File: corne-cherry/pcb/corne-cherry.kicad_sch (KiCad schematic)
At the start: 146 parts, among them J1 MJ-4PP-9, J2 OLED, J3 MJ-4PP-9, J4 OLED, SW1 SW_PUSH, SW10 SW_PUSH, SW11 SW_PUSH, SW12 SW_PUSH, SW13 SW_PUSH, SW14 SW_PUSH, SW15 SW_PUSH, SW16 SW_PUSH, SW17 SW_PUSH, SW18 SW_PUSH, SW19 SW_PUSH, SW2 SW_PUSH, SW20 SW_PUSH, SW21 SW_PUSH, SW22 SW_PUSH, SW23 SW_PUSH, SW24 SW_PUSH, SW25 SW_PUSH, SW26 SW_PUSH, SW27 SW_PUSH, SW28 SW_PUSH, SW29 SW_PUSH, SW3 SW_PUSH, SW30 SW_PUSH, SW31 SW_PUSH, SW32 SW_PUSH, SW33 SW_PUSH, SW34 SW_PUSH, SW35 SW_PUSH, SW36 SW_PUSH, SW37 SW_PUSH, SW38 SW_PUSH, SW39 SW_PUSH, SW4 SW_PUSH, SW40 SW_PUSH, SW41 SW_PUSH, SW42 SW_PUSH, SW5 SW_PUSH, SW6 SW_PUSH, SW7 SW_PUSH, SW8 SW_PUSH, SW9 SW_PUSH, U1 ProMicro, U2 ProMicro

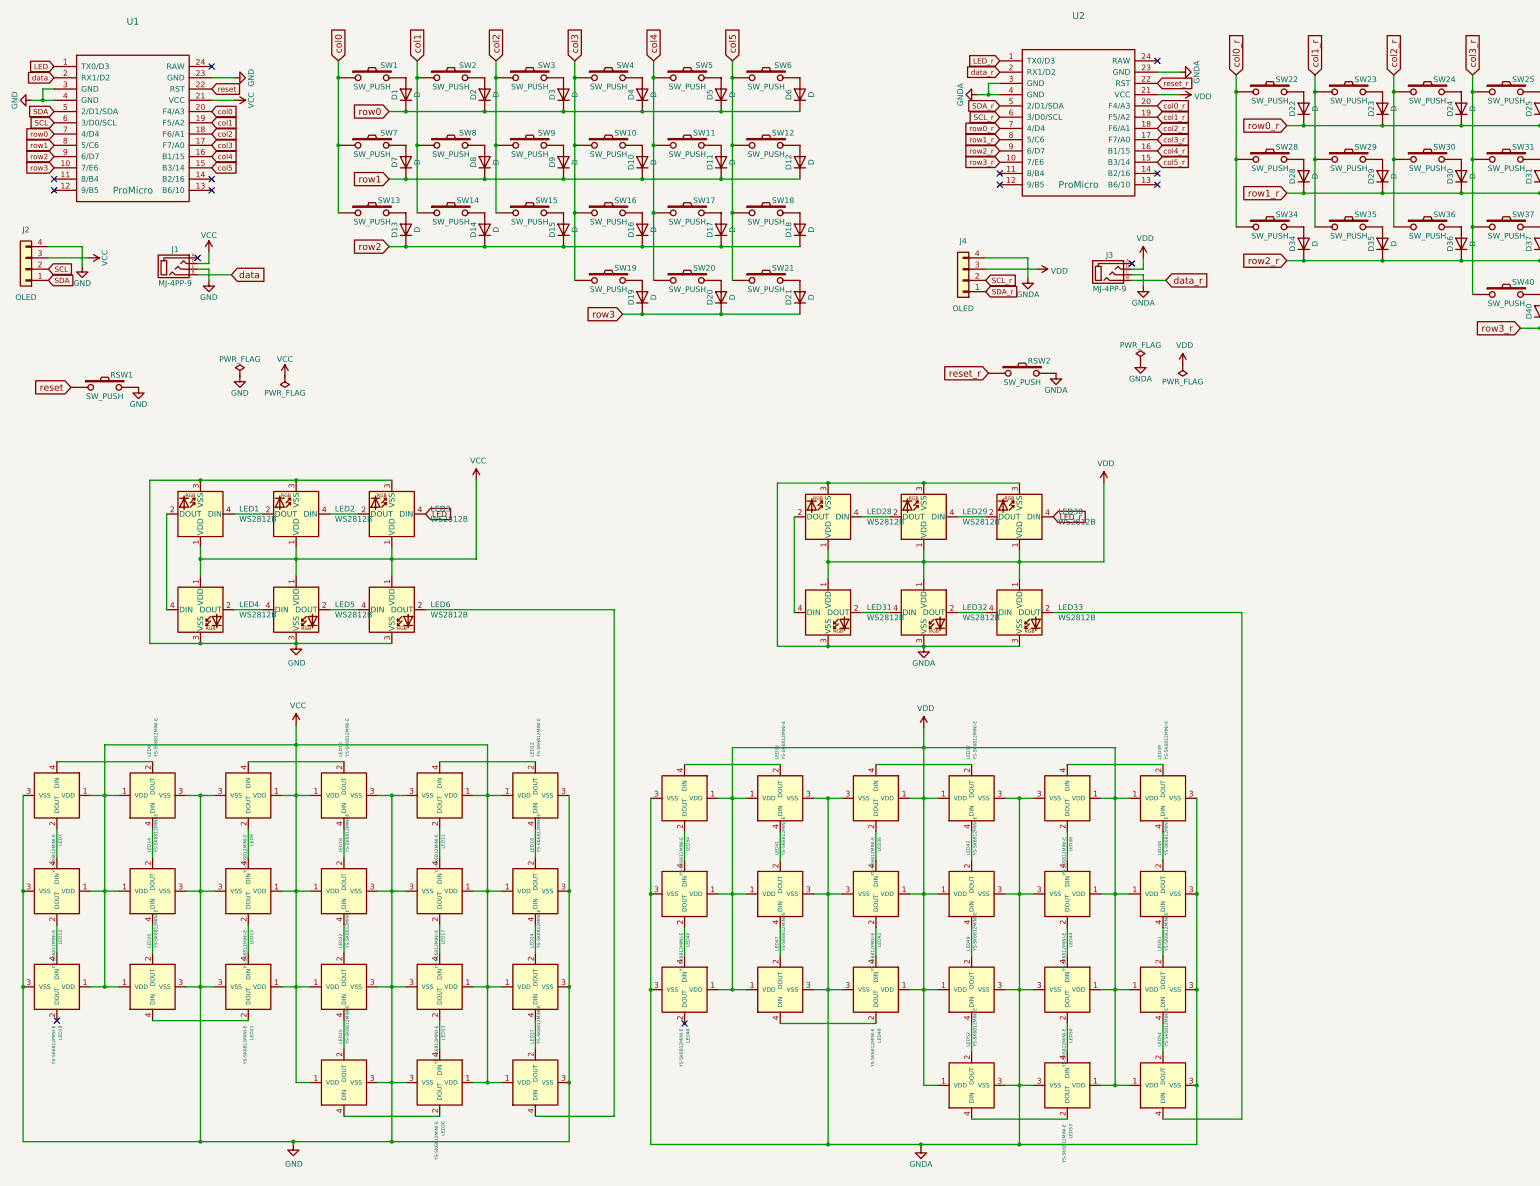
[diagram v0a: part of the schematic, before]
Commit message: fixed some traces added power switch added battery connections
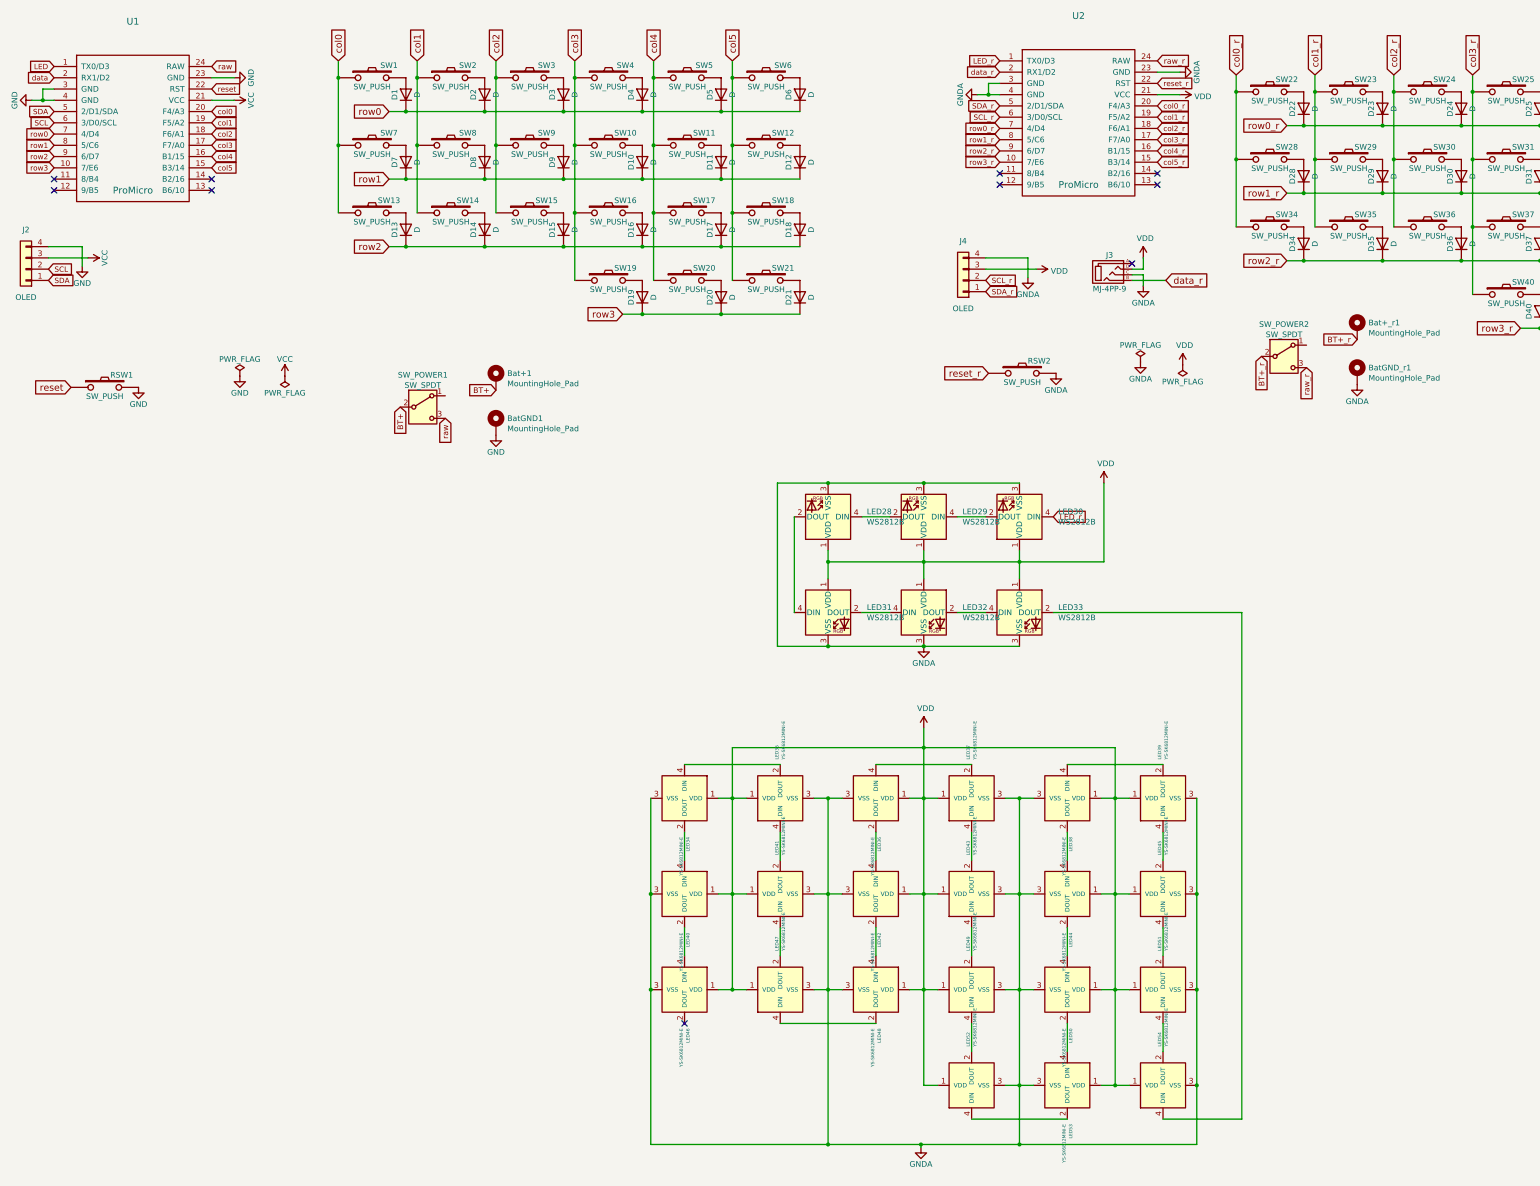
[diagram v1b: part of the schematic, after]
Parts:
- removed J1: MJ-4PP-9, kbd:MJ-4PP-9_1side, symbol kbd:MJ-4PP-9
- removed LED1, LED2, LED3, LED4, LED5, LED6: WS2812B, LED_SMD:LED_WS2812B_PLCC4_5.0x5.0mm_P3.2mm, symbol LED:WS2812B
- removed LED10, LED11, LED12, LED13, LED14, LED15, LED16, LED17, LED18, LED19, LED20, LED21, LED22, LED23, LED24, LED25, LED26, LED27, LED7, LED8, LED9: YS-SK6812MINI-E, kbd:YS-SK6812MINI-E, symbol kbd:YS-SK6812MINI-E
- added Bat+1, Bat+_r1, BatGND1, BatGND_r1: MountingHole_Pad, Connector_PinSocket_2.54mm:PinSocket_1x01_P2.54mm_Vertical, symbol Mechanical:MountingHole_Pad
- added SW_POWER1, SW_POWER2: SW_SPDT, Button_Switch_SMD:SW_SPDT_PCM12, symbol Switch:SW_SPDT
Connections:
- net GND: now also BatGND1.1
- net GNDA: now also BatGND_r1.1
- net raw: now reaches U1.24 (RAW)
- net raw: now also SW_POWER1.3 (C)
- net raw_r: now reaches U2.24 (RAW)
- net raw_r: now also SW_POWER2.3 (C)
- new net BT+: Bat+1.1, SW_POWER1.2 (B)
- new net BT+_r: Bat+_r1.1, SW_POWER2.2 (B)
- no-connect marks 14 -> 10
